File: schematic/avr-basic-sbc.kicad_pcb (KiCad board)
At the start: 2 copper layers, 94 x 55 mm, 38 parts, among them J1 DC-005 Power Jack, J2 PS/2 keyboard port, J3 RCA Video Jack, J4 Port B, J5 Port A, J6 Port C, J7 Port D, J8 USBasp header, J9 Power output header, U1 ATmega1284P-P, U2 L7805, U3 25LC640, Y1 16 MHz

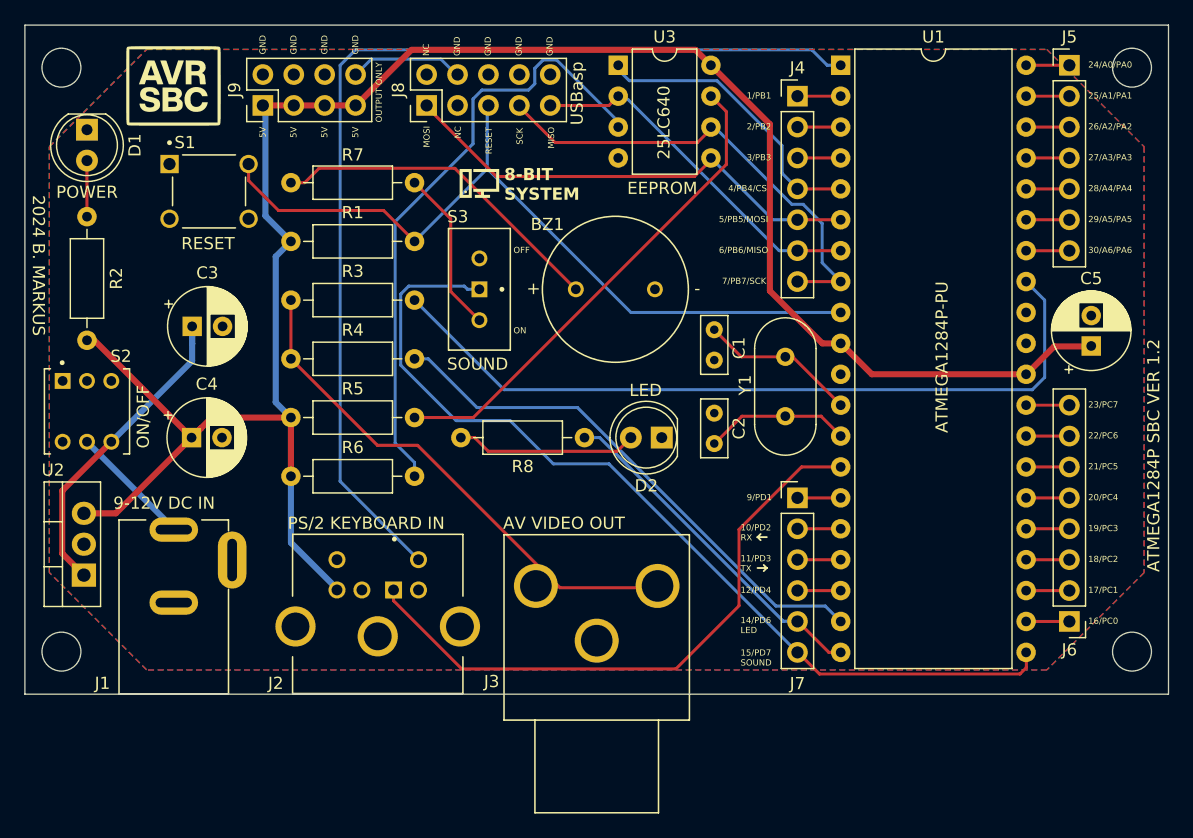
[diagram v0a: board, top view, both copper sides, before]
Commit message: Schematic: Update to v1.3, schottky diode added to ISP header for protection, decoupling capacitors added
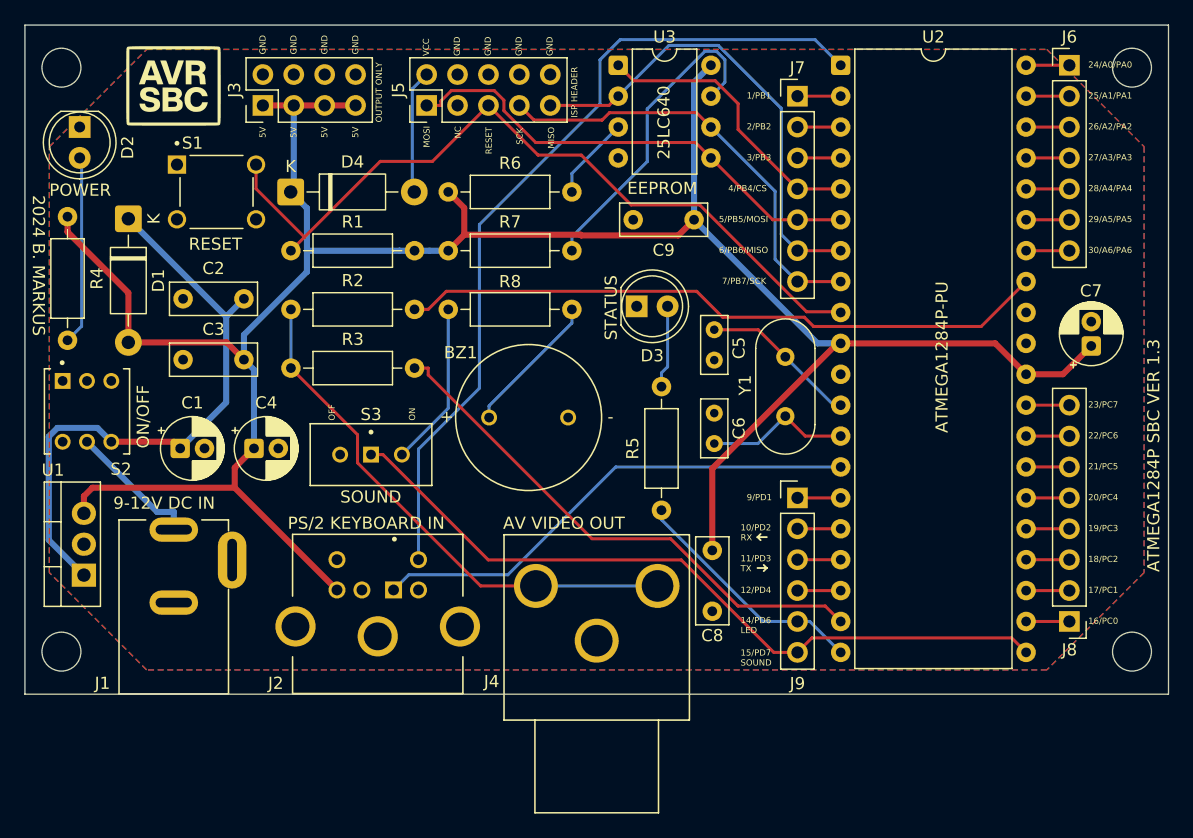
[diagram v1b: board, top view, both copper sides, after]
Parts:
- removed GRAPHICS2: LOGO, LOGO
- added C1: 10uF, Capacitor_THT:CP_Radial_D5.0mm_P2.00mm, F.Cu at (12.8, 34.8)
- added C2: 0.33uF, StockLib:C_100nF_L7.0mm_W2.5mm_P5.00mm, F.Cu at (13.0, 22.5)
- added C8: 0.1uF, StockLib:C_100nF_L7.0mm_W2.5mm_P5.00mm, F.Cu at (56.5, 48.2)
- added C9: 0.1uF, StockLib:C_100nF_L7.0mm_W2.5mm_P5.00mm, F.Cu at (50.0, 16.0)
- added D1: 1N4001, Diode_THT:D_DO-41_SOD81_P10.16mm_Horizontal, F.Cu at (8.50, 15.9)
- added D4: 1N5819, Diode_THT:D_DO-41_SOD81_P10.16mm_Horizontal, F.Cu at (21.8, 13.7)
- C3: value 0.33uF -> 0.1uF; footprint Capacitor_THT:CP_Radial_D6.3mm_P2.50mm -> StockLib:C_100nF_L7.0mm_W2.5mm_P5.00mm
- C4: value 0.1uF -> 10uF; footprint Capacitor_THT:CP_Radial_D6.3mm_P2.50mm -> Capacitor_THT:CP_Radial_D5.0mm_P2.00mm
- C7: renamed from C5; footprint Capacitor_THT:CP_Radial_D6.3mm_P2.50mm -> Capacitor_THT:CP_Radial_D5.0mm_P2.00mm
- moved R6 26.7 mm to (34.8, 13.7)
- moved R7 18.9 mm to (34.8, 18.5)
- moved S3 16.2 mm to (28.4, 35.3), turned to 180 degrees
- moved BZ1 12.7 mm to (41.4, 32.3)
- moved D3 11.0 mm to (50.3, 23.1), turned to 0 degrees
- moved R8 10.8 mm to (34.8, 23.4), turned to 0 degrees
- moved R5 8.70 mm to (52.3, 39.9), turned to 90 degrees
- moved C4 5.21 mm to (18.8, 34.8)
- moved C3 2.83 mm to (13.0, 27.5)
- moved R4 1.60 mm to (3.50, 25.9)
- moved R1 0.76 mm to (21.9, 18.5)
- moved R3 0.76 mm to (21.9, 28.2)
- moved R2 0.76 mm to (21.9, 23.4)
- moved D2 0.64 mm to (4.50, 8.38)
- moved S1 0.62 mm to (15.7, 13.7)
- renumbered C1 to C5, C2 to C6, D1 to D2, D2 to D3, J9 to J3, J3 to J4, J8 to J5, J5 to J6, J4 to J7, J6 to J8, J7 to J9, R3 to R2, R4 to R3, R2 to R4, R8 to R5, R5 to R7, R7 to R8, U2 to U1, U1 to U2
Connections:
- C3 pad 1: /POWER IN 2 -> GND
- C3 pad 2: GND -> +5V
- D2 pad 2: Net-(D1-A) -> Net-(D2-A)
- J5 pad 2: unconnected-(J8-Pin_2-Pad2) -> Net-(D4-A)
- R1 pad 1: +5V -> RESET
- R1 pad 2: RESET -> +5V
- R4 pad 1: +5V -> Net-(D2-A)
- R4 pad 2: Net-(D1-A) -> +5V
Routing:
- net Net-(U3-~{WP}): track 51.2 -> 6.91 mm
- net +5V: track 166.4 -> 202.0 mm
- net /POWER IN 2: track 27.0 -> 50.2 mm
- net Clock: track 85.5 -> 68.6 mm
- net Net-(BZ1-+): track 28.0 -> 11.7 mm
- net Net-(D2-A): track 0.00 -> 15.5 mm
- net Net-(J9-Pin_6): track 76.1 -> 61.6 mm
- net Net-(U3-~{HOLD}): track 40.4 -> 26.3 mm
- net Net-(D4-A): track 0.00 -> 10.2 mm
- net Video: track 63.8 -> 53.6 mm
- net Data: track 50.5 -> 40.9 mm
- net MISO: track 29.6 -> 39.0 mm
- net GND: track 9.30 -> 0.00 mm
- net Net-(J9-Pin_5): track 28.4 -> 20.0 mm
- net Net-(D3-A): track 14.9 -> 6.81 mm
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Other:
- board text added: "ATMEGA1284P SBC VER 1.3"
- board text added: "ISP HEADER"
- board text added: "STATUS"
- board text added: "VCC"
- board text removed: "8-BIT SYSTEM"
- board text removed: "ATMEGA1284P SBC VER 1.2"
- board text removed: "LED"
- board text removed: "USBasp"

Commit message: PCB updated
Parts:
- moved R5 0.80 mm to (51.6, 39.6)
- moved S1 0.76 mm to (15.0, 13.7)
- moved BZ1 0.51 mm to (41.4, 32.8)
- moved S3 0.51 mm to (28.4, 34.8)
- moved C2 0.50 mm to (13.5, 22.5)
- moved C3 0.50 mm to (13.5, 27.5)
- moved D2 0.33 mm to (4.83, 8.38)
- moved R4 0.31 mm to (3.81, 25.9)
- moved D1 0.14 mm to (8.64, 15.9)
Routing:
- net /POWER IN 2: track 50.2 -> 51.1 mm
- net Net-(J9-Pin_5): track 20.0 -> 20.9 mm
- net Sync: track 44.0 -> 44.8 mm
- net Net-(R8-Pad1): track 13.5 -> 13.0 mm
- net Net-(BZ1-+): track 11.7 -> 12.2 mm

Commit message: PCB reverted to release version v1.2
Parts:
- removed the C1 at (12.8, 34.8)
- removed the C2 at (13.5, 22.5)
- removed C8, C9: 0.1uF, StockLib:C_100nF_L7.0mm_W2.5mm_P5.00mm
- removed the D1 at (8.64, 15.9)
- removed D4: 1N5819, Diode_THT:D_DO-41_SOD81_P10.16mm_Horizontal
- added GRAPHICS2: LOGO, LOGO, F.Cu at (37.4, 13.0)
- C3: value 0.1uF -> 0.33uF; footprint StockLib:C_100nF_L7.0mm_W2.5mm_P5.00mm -> Capacitor_THT:CP_Radial_D6.3mm_P2.50mm
- C4: value 10uF -> 0.1uF; footprint Capacitor_THT:CP_Radial_D5.0mm_P2.00mm -> Capacitor_THT:CP_Radial_D6.3mm_P2.50mm
- C5: renamed from C7; footprint Capacitor_THT:CP_Radial_D5.0mm_P2.00mm -> Capacitor_THT:CP_Radial_D6.3mm_P2.50mm
- moved R6 26.7 mm to (21.9, 37.1)
- moved R5 18.9 mm to (21.9, 32.3)
- moved S3 15.8 mm to (37.4, 21.7), turned to 90 degrees
- moved BZ1 13.2 mm to (48.5, 21.7)
- moved D2 11.0 mm to (52.3, 33.9), turned to 180 degrees
- moved R7 10.8 mm to (32.0, 13.0), turned to 180 degrees
- moved R8 7.98 mm to (46.0, 33.9), turned to 180 degrees
- moved C4 5.21 mm to (13.7, 33.9)
- moved C3 2.75 mm to (13.7, 24.8)
- moved R2 1.29 mm to (5.10, 25.9)
- moved R1 0.76 mm to (21.9, 17.8)
- moved R4 0.76 mm to (21.9, 27.4)
- moved R3 0.76 mm to (21.9, 22.6)
- moved D1 0.35 mm to (5.10, 8.60)
- moved S1 0.15 mm to (15.1, 13.7)
- renumbered C5 to C1, C6 to C2, D2 to D1, D3 to D2, J4 to J3, J7 to J4, J6 to J5, J8 to J6, J9 to J7, J5 to J8, J3 to J9, R4 to R2, R2 to R3, R3 to R4, R7 to R5, R8 to R7, R5 to R8, U2 to U1, U1 to U2
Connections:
- C3 pad 1: GND -> /POWER IN 2
- C3 pad 2: +5V -> GND
- D1 pad 2: Net-(D2-A) (its old number) -> Net-(D1-A)
- J8 pad 2: Net-(D4-A) -> unconnected-(J8-Pin_2-Pad2)
- R1 pad 1: RESET -> +5V
- R1 pad 2: +5V -> RESET
- R2 pad 1: Net-(D2-A) (its old number) -> +5V
- R2 pad 2: +5V -> Net-(D1-A)
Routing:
- net Net-(U3-~{WP}): track 6.91 -> 51.2 mm
- net +5V: track 201.9 -> 166.4 mm
- net /POWER IN 2: track 51.1 -> 27.0 mm
- net Clock: track 68.6 -> 85.5 mm
- net Net-(BZ1-+): track 12.2 -> 28.0 mm
- net Net-(D2-A) (its old number): track 15.6 -> 0.00 mm
- net Net-(J7-Pin_6): track 61.8 -> 76.1 mm
- net Net-(U3-~{HOLD}): track 26.3 -> 40.4 mm
- net Net-(D4-A): track 10.2 -> 0.00 mm
- net Video: track 53.6 -> 63.8 mm
- net Data: track 40.9 -> 50.5 mm
- net MISO: track 39.0 -> 29.6 mm
- net GND: track 0.00 -> 9.30 mm
- net Net-(D2-A): track 6.87 -> 14.9 mm
- net Net-(J7-Pin_5): track 20.9 -> 28.4 mm
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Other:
- board text added: "8-BIT SYSTEM"
- board text added: "ATMEGA1284P SBC VER 1.2"
- board text added: "LED"
- board text added: "USBasp"
- board text removed: "ATMEGA1284P SBC VER 1.3"
- board text removed: "ISP HEADER"
- board text removed: "STATUS"
- board text removed: "VCC"
